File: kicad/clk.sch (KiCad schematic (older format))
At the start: 61 parts

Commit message: cleaned clk.sch and some details on ethercat/net
I've cleaned up a lot from clk, I'm planning to use 25mhz external clk
and the ethernet/cat interfaces will eat from C2000, not from same clk.
I think it could work, cose the uC is designed in that way to use
GPIO154 to provide the clk.. will see...
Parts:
- removed C? (x5): 0.1uF, symbol servo:Capacitor
- removed C?: 0.01uF, symbol servo:Capacitor
- removed IC? (x2): (no value), symbol servo:TPS3702
- removed IC?: (no value), symbol servo:MicroSD_4Shield
- removed J?: (no value), symbol servo:Header_4x2
- removed R? (x2): 1.5M, symbol servo:Resistor
- removed R? (x14): 0e, symbol servo:Resistor
- removed R? (x4): 10.0, symbol servo:Resistor
- removed R? (x3): 10.0k, symbol servo:Resistor
- removed R? (x3): 2.2k, symbol servo:Resistor
- removed S?: (no value), symbol servo:SW_2SPST
- removed TP? (x3): (no value), symbol servo:CMP-0078143-2
- removed U?: SN74LVC2G07DBVR, symbol servo:SN74LVC2G07
- removed U?: CDCLVC1104, symbol servo:CDCLVC1104
- removed Y?: (no value), symbol servo:OSC_4P_1_TRI-STATE
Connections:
- net labels removed: 20MHZ_CLK, 25MHZ_CLK, 50 Ohm, ENET_PHY_CLK, F2838x_25MHZ_CLK, HSEC_GPIO26, HSEC_GPIO27, HSEC_GPIO8, HSEC_GPIO9, MCU_GPIO100, MCU_GPIO101, MCU_GPIO102, MCU_GPIO103, MCU_GPIO107, MCU_GPIO154, MCU_GPIO26, MCU_GPIO27, MCU_GPIO8, MCU_GPIO9, P0_25MHZ_CLK, P0_PHY_CLK, P1_25MHZ_CLK, P1_PHY_CLK
- wire segments 208 -> 46
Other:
- note added: "Boot Mode to Flash/USB\n"
- note added: "Multiporpouse \nLEDs"
- note added: "Reset\n"
- note removed: "20MHz Clock"
- note removed: "Boot Mode Selection Switch"
- note removed: "Clock Source Selection"
- note removed: "FSI Header"
- note removed: "LEDs"
- note removed: "Micro-SD Card"
- note removed: "Place near U5"
- note removed: "Reset & Voltage Monitoring"
- moved on the sheet: C?, D?, R?, S?, TP?, Y?

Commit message: cleaning power, added ac/dc to 15v
I've added the ac/dc power supply based on encapsulated off load power
supply and chainde linear regulator for 5, 3v3 and 1v2 for cold gnd and
5v and 3v3 for hot gnd.
I'll next join some sheet 'cose some of those are almost empty
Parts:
- removed R?: 0e, symbol servo:Resistor
- S?, TP? (x3), Y?: value (none) -> ~
- U1_?: value (none) -> ~; symbol servo:TMS320F28388_3 -> servo:TMS320F28388
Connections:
- wire segments 46 -> 43
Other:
- moved on the sheet: C?, D?, R?, S?, TP?, Y?

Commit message: ok, it's enough cleaned to mix with power interface
I think it's time to mix with power interfaces.. It's enough cleaned
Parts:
- removed R?: 2.2k, symbol servo:Resistor
- added D?: green, symbol servo:LED_A2_K1
- added D?: blue, symbol servo:LED_A2_K1
- added J?: Conn_02x05_Counter_Clockwise, symbol Connector_Generic:Conn_02x05_Counter_Clockwise
- added R? (x2): 1.0k, symbol servo:Resistor
- U1_?: value ~ -> TMS320F28388DZWTS
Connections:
- net labels added: 3V3, 5VC, MCU_GPIO28, MCU_GPIO29
- net labels removed: TMS320F28388DZWTS, VDD_3V3
- wire segments 43 -> 71
- no-connect marks 3 -> 2
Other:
- note added: "Boot Mode to\n Flash/USB\n"
- note added: "IDC connector to plug \nan external isolated jtag interface"
- note added: "SCI leds\n"
- note removed: "Boot Mode to Flash/USB\n"
- moved on the sheet: C?, D?, R?, S?, TP?, U1_?C, Y?

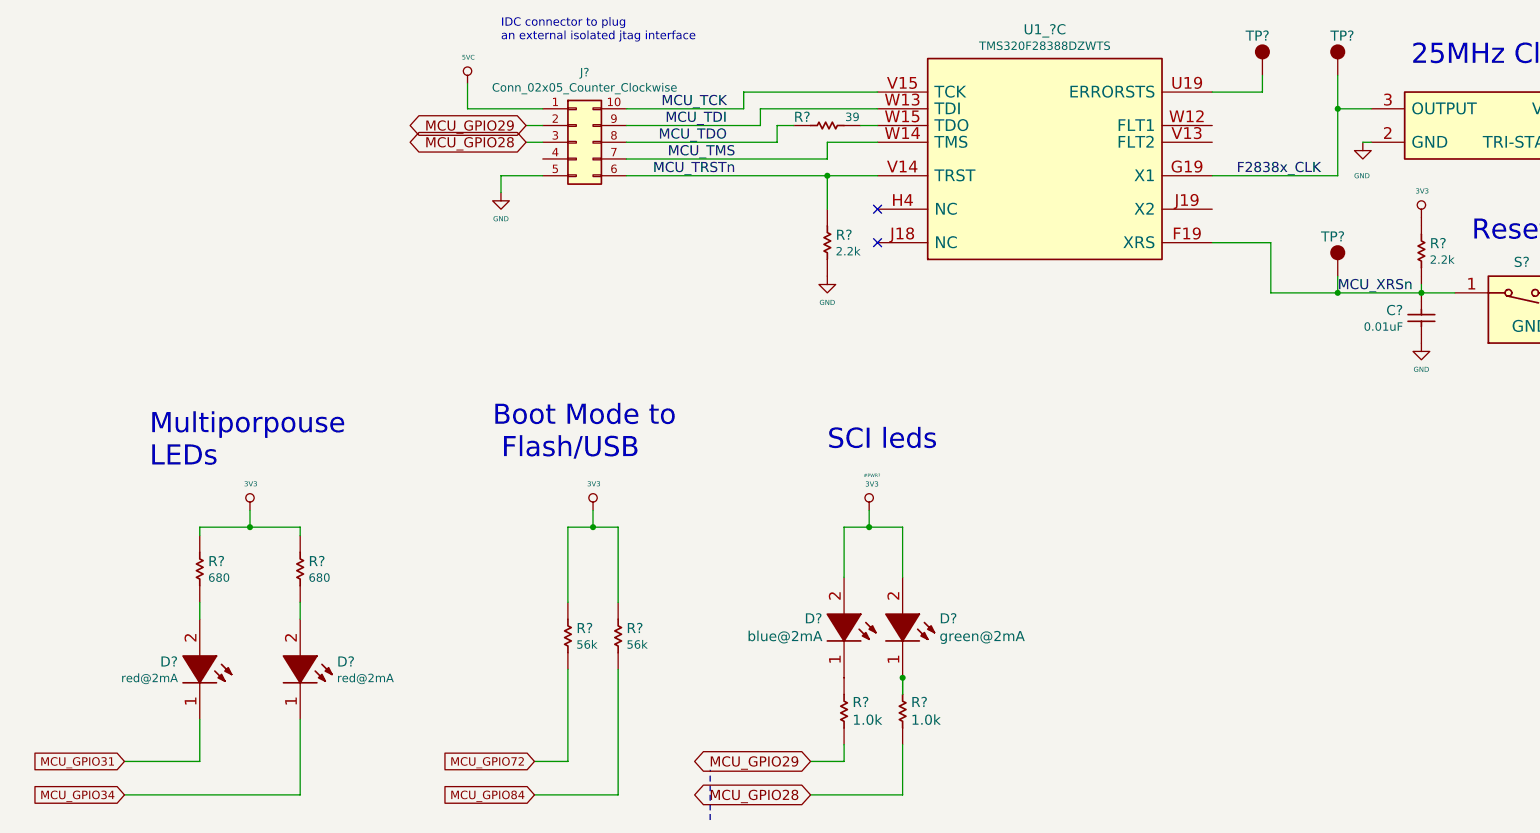
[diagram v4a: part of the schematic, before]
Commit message: I've connected interfaces to gpio and change some muxes
I've changed some muxes reading the datasheet to group same kind of
signals, now it's time to add encoders input
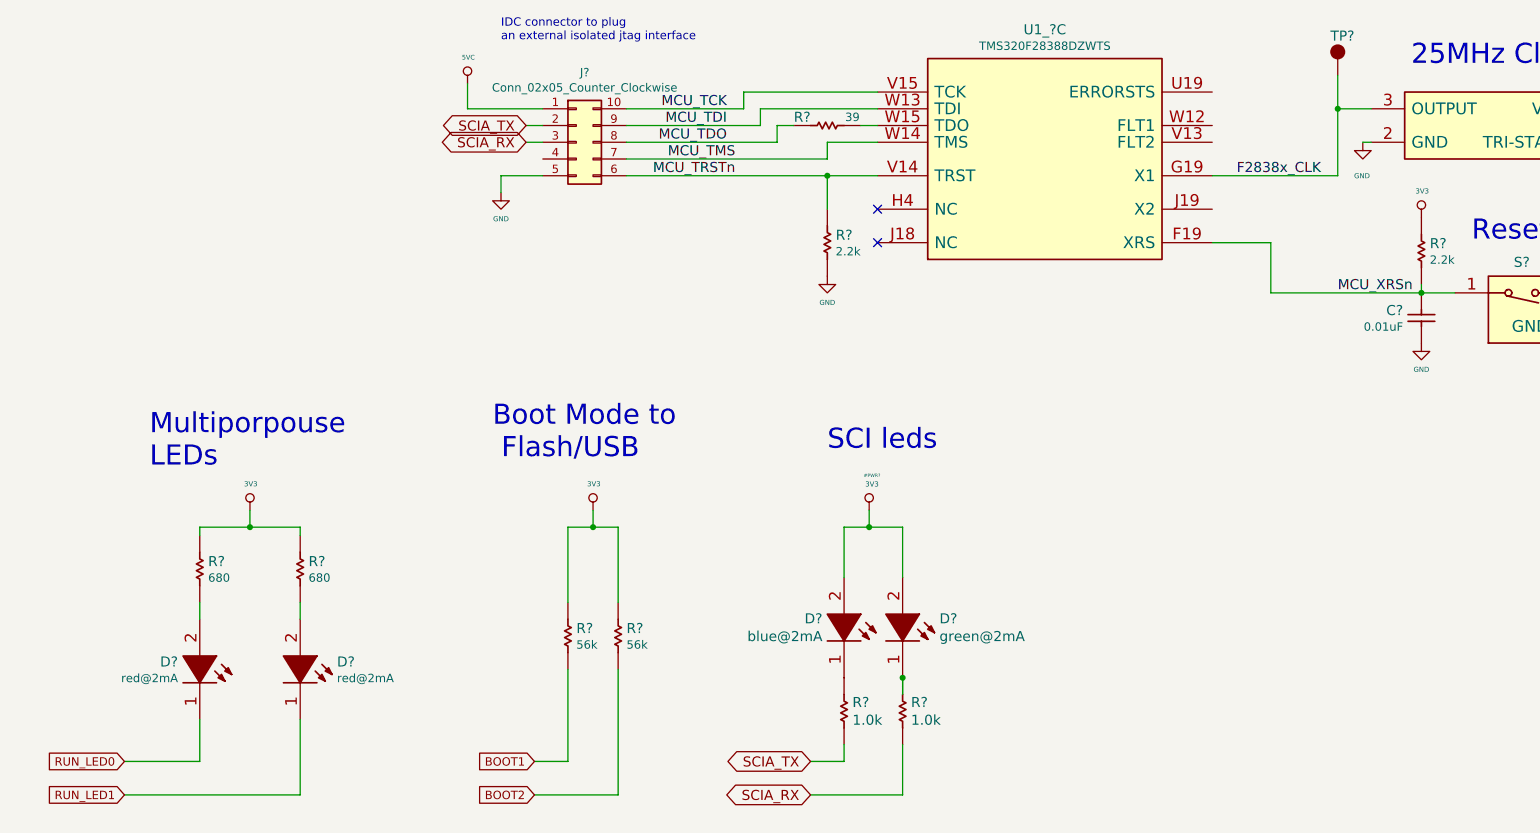
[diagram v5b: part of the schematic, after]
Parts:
- removed TP? (x2): ~, symbol servo:CMP-0078143-2
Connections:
- net MCU_GPIO28 renamed SCIA_RX
- net MCU_GPIO29 renamed SCIA_TX
- net MCU_GPIO31 renamed RUN_LED0
- net MCU_GPIO34 renamed RUN_LED1
- net MCU_GPIO72 renamed BOOT1
- net MCU_GPIO84 renamed BOOT2
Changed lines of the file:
@@
 Comment4 ""
 $EndDescr
-Wire Notes Line
-	4900 5850 4900 5550
 $Comp
 L servo:3V3 #PWR_?
@@
 Text Label 8650 2700 0    60   ~ 0
 MCU_XRSn
-Wire Wire Line
-	8200 1500 7900 1500
-Wire Wire Line
-	8200 1400 8200 1500
 Text Label 8550 2000 2    60   ~ 0
 F2838x_CLK
@@
 $EndComp
 $Comp
-L servo:CMP-0078143-2 TP?
-U 1 1 5DB38F59
-P 8200 1300
-F 0 "TP?" H 8100 1400 60  0000 L BNN
-F 1 "~" H 8200 1300 50  0001 C CNN
-F 2 "" H 8200 1300 50  0001 C CNN
-F 3 "" H 8200 1300 50  0001 C CNN
-	1    8200 1300
-	1    0    0    -1
-$EndComp
-$Comp
-L servo:CMP-0078143-2 TP?
-U 1 1 5DB38F58
-P 8650 2500
-F 0 "TP?" H 8550 2600 60  0000 L BNN
-F 1 "~" H 8650 2500 50  0001 C CNN
-F 2 "" H 8650 2500 50  0001 C CNN
-F 3 "" H 8650 2500 50  0001 C CNN
-	1    8650 2500
-	1    0    0    -1
-$EndComp
-$Comp
 L servo:Switch_PushButton_GND3 S?
 U 1 1 5DB38F55
@@
 	1400 5700 2450 5700
 Text GLabel 1400 5500 0    50   Input ~ 0
-MCU_GPIO31
+RUN_LED0
 Text GLabel 1400 5700 0    50   Input ~ 0
-MCU_GPIO34
+RUN_LED1
 Text GLabel 3850 5500 0    50   Input ~ 0
-MCU_GPIO72
+BOOT1
 Text GLabel 3850 5700 0    50   Input ~ 0
-MCU_GPIO84
+BOOT2
 Wire Wire Line
 	1850 4100 2150 4100
@@
 	4200 4000 4200 4100
 Connection ~ 9150 2700
-Wire Wire Line
-	9150 2700 8650 2700
 Wire Wire Line
 	8250 2400 7900 2400
@@
 Text Notes 3650 1200 0    50   ~ 0
 IDC connector to plug \nan external isolated jtag interface
-Text GLabel 5500 5500 0    60   BiDi ~ 0
-MCU_GPIO29
-Text GLabel 5500 5700 0    60   BiDi ~ 0
-MCU_GPIO28
 Wire Wire Line
 	3900 1800 3800 1800
@@
 Wire Wire Line
 	6050 5700 6050 5400
-Text GLabel 3800 1700 0    60   BiDi ~ 0
-MCU_GPIO29
-Text GLabel 3800 1800 0    60   BiDi ~ 0
-MCU_GPIO28
 $Comp
 L servo:5VC #PWR?
@@
 	8650 1600 8650 2000
 Wire Wire Line
-	8650 2600 8650 2700
-Connection ~ 8650 2700
-Wire Wire Line
 	9150 2700 9350 2700
-Wire Wire Line
-	8650 2700 8250 2700
 Wire Wire Line
 	8250 2700 8250 2400
@@
 Wire Wire Line
 	1850 5250 1850 5500
+Text GLabel 3800 1700 0    60   BiDi ~ 0
+SCIA_TX
+Text GLabel 3800 1800 0    60   BiDi ~ 0
+SCIA_RX
+Text GLabel 5500 5500 0    60   BiDi ~ 0
+SCIA_TX
+Text GLabel 5500 5700 0    60   BiDi ~ 0
+SCIA_RX
+Wire Wire Line
+	8250 2700 9150 2700
 $EndSCHEMATC

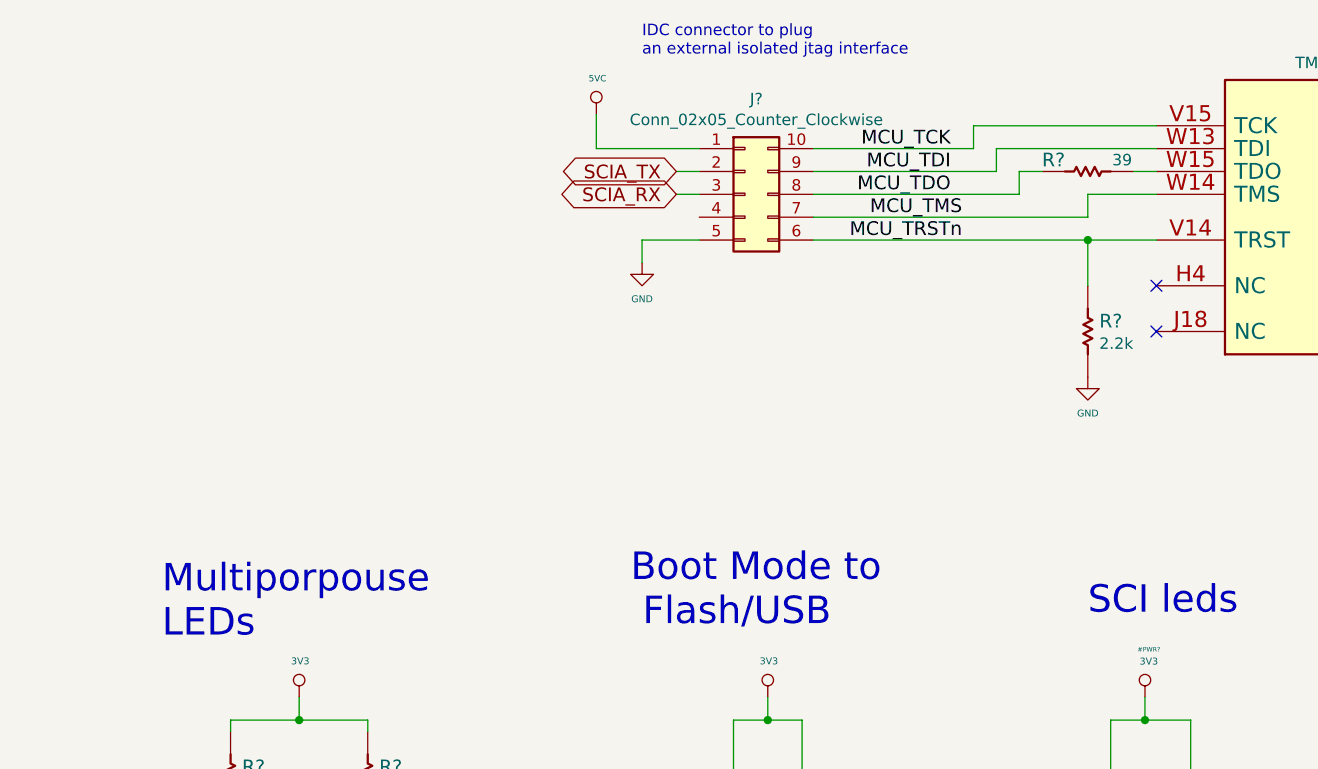
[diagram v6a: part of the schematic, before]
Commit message: added shunt using sigma delta, just fot 1 channel
I've added a sigma delta isolated sampler for use with shunt in phase
measurement. 'cose it seems is the best accuracy method for current
measurement, but it implies a lot of componentes, 8 PWM lines to
generate the sigma delta clk, or maybe I'd use only one clk for all
sigma deltas, ..I've to think about it, but it seems that should be
better than Hall.. working on that
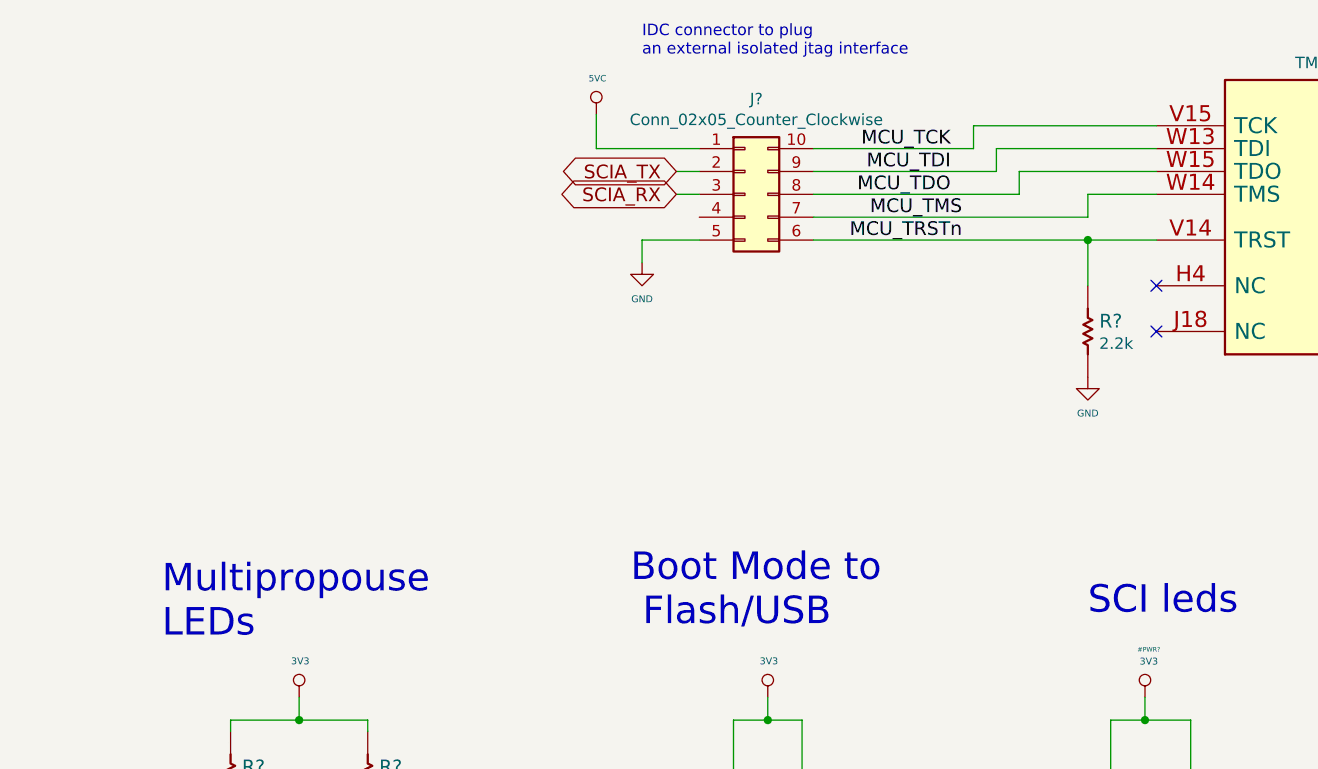
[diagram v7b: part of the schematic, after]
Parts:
- removed R?: 39, symbol servo:Resistor
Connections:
- net MCU_TDO: now also U1_?.W15 (TDO)
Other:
- note added: "Multipropouse\nLEDs"
- note removed: "Multiporpouse \nLEDs"
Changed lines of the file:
@@
 $Descr A4 11693 8268
 encoding utf-8
-Sheet 6 14
+Sheet 6 15
 Title "clk"
 Date "25 10 2019"
@@
 	2450 5700 2450 5250
 Text Notes 1550 3750 0    120  ~ 0
-Multiporpouse \nLEDs
+Multipropouse\nLEDs
 Text Notes 3600 3700 0    120  ~ 0
 Boot Mode to\n Flash/USB\n
@@
 Wire Wire Line
 	5600 2000 5600 2200
-Wire Wire Line
-	5300 1700 5400 1700
-Wire Wire Line
-	5900 1700 5800 1700
 Wire Wire Line
 	1400 5500 1850 5500
@@
 	1    1850 4350
 	0    1    1    0
-$EndComp
-$Comp
-L servo:Resistor R?
-U 1 1 5DB38F5B
-P 5600 1700
-F 0 "R?" H 5450 1750 60  0000 C CNN
-F 1 "39" H 5750 1750 50  0000 C CNN
-F 2 "" H 5600 1700 50  0001 C CNN
-F 3 "" H 5600 1700 50  0001 C CNN
-F 4 "39" V 5500 1700 60  0001 C CNN "ValueDisplayed"
-	1    5600 1700
-	1    0    0    -1
 $EndComp
 $Comp
@@
 Wire Wire Line
 	8250 2700 9150 2700
+Wire Wire Line
+	5300 1700 5900 1700
 $EndSCHEMATC
